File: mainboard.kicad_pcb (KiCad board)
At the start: 2 copper layers, 81.3 x 72.5 mm, 56 parts, among them J1 Screw_Terminal_1x02, Q1 SQ2309ES, U1 AT90CAN128-16MU, U2 MCP2551-I/SN, Y1 Crystal

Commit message: Did some power things
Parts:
- moved Q1 10.3 mm to (130.2, 99.7), turned to 180 degrees
- moved C9 8.55 mm to (122.2, 101.3)
- moved C3 8.52 mm to (122.2, 102.7)
- moved R8 6.86 mm to (115.2, 100.5)
- moved D2 6.85 mm to (115.2, 105.3)
- moved J1 1.79 mm to (131.8, 104.9)
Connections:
- R8 pad 1: (no net) -> +5V
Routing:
- net +5V: track 265.4 -> 224.8 mm, vias 13 -> 11
- net GND: track 106.5 -> 72.7 mm
- net Net-(J1-Pad2): track 7.44 -> 0.00 mm
- net Net-(D2-Pad2): track 1.85 -> 0.00 mm
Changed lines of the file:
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@@
 (kicad_pcb (version 4) (host pcbnew 4.0.6-e0-6349~53~ubuntu16.04.1)
   (general
-    (links 196)
-    (no_connects 5)
+    (links 197)
+    (no_connects 60)
     (area 62.027999 36.881999 143.458001 109.549001)
     (thickness 1.6)
     (drawings 182)
-    (tracks 629)
+    (tracks 601)
     (zones 0)
     (modules 56)
@@
   )
   (module Connectors_Terminal_Blocks:TerminalBlock_Pheonix_MPT-2.54mm_2pol (layer F.Cu)
-    (at 130.18 105.712 180)
+    (at 131.78 104.912 180)
     (descr "2-way 2.54mm pitch terminal block, Phoenix MPT series")
     (fp_text reference J1 (at 1.27 -4.50088 180) (layer F.SilkS) hide
@@
   )
   (module LEDs:LED_1206 (layer F.Cu)
-    (at 108.331 105.029 90)
+    (at 115.18 105.312 90)
     (descr "LED 1206 smd package")
     (tags "LED led 1206 SMD smd SMT smt smdled SMDLED smtled SMTLED")
@@
   )
   (module Resistors_SMD:R_1206 (layer F.Cu)
-    (at 108.331 100.076 270)
+    (at 115.18 100.512 270)
     (descr "Resistor SMD 1206, reflow soldering, Vishay (see dcrcw.pdf)")
     (tags "resistor 1206")
@@
     (fp_line (start 2.15 1.1) (end 2.15 -1.11) (layer F.CrtYd) (width 0.05))
     (fp_line (start 2.15 1.1) (end -2.15 1.1) (layer F.CrtYd) (width 0.05))
-    (pad 1 smd rect (at -1.45 0 270) (size 0.9 1.7) (layers F.Cu F.Paste F.Mask))
+    (pad 1 smd rect (at -1.45 0 270) (size 0.9 1.7) (layers F.Cu F.Paste F.Mask)
+      (net 4 +5V))
     (pad 2 smd rect (at 1.45 0 270) (size 0.9 1.7) (layers F.Cu F.Paste F.Mask)
       (net 63 "Net-(D2-Pad2)"))
@@
   )
   (module Capacitors_SMD:CP_Elec_6.3x4.5 (layer F.Cu)
-    (at 113.665 102.997 270)
+    (at 122.18 102.712 270)
     (descr "SMT capacitor, aluminium electrolytic, 6.3x4.5")
     (attr smd)
@@
   )
   (module Capacitors_THT:CP_Radial_D7.5mm_P2.50mm (layer F.Cu)
-    (at 113.665 102.108 270)
+    (at 122.18 101.312 270)
     (descr "CP, Radial series, Radial, pin pitch=2.50mm, , diameter=7.5mm, Electrolytic Capacitor")
     (tags "CP Radial series Radial pin pitch 2.50mm  diameter 7.5mm Electrolytic Capacitor")
@@
   )
   (module TO_SOT_Packages_SMD:SOT-23 (layer F.Cu)
-    (at 120.65 103.632 270)
+    (at 130.18 99.712 180)
     (descr "SOT-23, Standard")
     (tags SOT-23)
     (attr smd)
-    (fp_text reference Q1 (at -2.52 -0.13 360) (layer F.SilkS)
+    (fp_text reference Q1 (at -2.52 -0.13 270) (layer F.SilkS)
       (effects (font (size 1 1) (thickness 0.15)))
     )
-    (fp_text value SQ2309ES (at 0 2.5 270) (layer F.Fab) hide
+    (fp_text value SQ2309ES (at 0 2.5 180) (layer F.Fab) hide
       (effects (font (size 1 1) (thickness 0.15)))
     )
-    (fp_text user %R (at 0 0 360) (layer F.Fab)
+    (fp_text user %R (at 0 0 270) (layer F.Fab)
       (effects (font (size 0.5 0.5) (thickness 0.075)))
     )
@@
     (fp_line (start 0.76 -1.58) (end -1.4 -1.58) (layer F.SilkS) (width 0.12))
     (fp_line (start 0.76 1.58) (end -0.7 1.58) (layer F.SilkS) (width 0.12))
-    (pad 1 smd rect (at -1 -0.95 270) (size 0.9 0.8) (layers F.Cu F.Paste F.Mask)
+    (pad 1 smd rect (at -1 -0.95 180) (size 0.9 0.8) (layers F.Cu F.Paste F.Mask)
       (net 2 GND))
-    (pad 2 smd rect (at -1 0.95 270) (size 0.9 0.8) (layers F.Cu F.Paste F.Mask)
+    (pad 2 smd rect (at -1 0.95 180) (size 0.9 0.8) (layers F.Cu F.Paste F.Mask)
       (net 4 +5V))
-    (pad 3 smd rect (at 1 0 270) (size 0.9 0.8) (layers F.Cu F.Paste F.Mask)
+    (pad 3 smd rect (at 1 0 180) (size 0.9 0.8) (layers F.Cu F.Paste F.Mask)
       (net 64 "Net-(J1-Pad2)"))
     (model ${KISYS3DMOD}/TO_SOT_Packages_SMD.3dshapes/SOT-23.wrl
@@
   (gr_line (start 62.23 36.957) (end 143.383 36.957) (angle 90) (layer Edge.Cuts) (width 0.15))
   (gr_line (start 62.103 109.474) (end 62.103 37.084) (angle 90) (layer Edge.Cuts) (width 0.15))
-  (gr_text 5V (at 125.38 105.912 90) (layer F.SilkS)
+  (gr_text 5V (at 126.98 105.712 90) (layer F.SilkS)
     (effects (font (size 1 1) (thickness 0.1)))
   )
@@
     (effects (font (size 0.8 0.7) (thickness 0.125)))
   )
-  (gr_text GND (at 132.38 106.112 270) (layer F.SilkS)
+  (gr_text GND (at 133.98 105.512 270) (layer F.SilkS)
     (effects (font (size 1 1) (thickness 0.1)))
   )
@@
   (segment (start 64.008 80.645) (end 66.675 83.312) (width 0.25) (layer F.Cu) (net 2))
   (segment (start 64.008 64.9732) (end 63.9826 64.9478) (width 0.5) (layer F.Cu) (net 2))
-  (segment (start 121.6 102.632) (end 130.1 102.632) (width 0.5) (layer F.Cu) (net 2))
-  (segment (start 130.18 102.712) (end 130.18 105.712) (width 0.5) (layer F.Cu) (net 2))
-  (segment (start 130.1 102.632) (end 130.18 102.712) (width 0.5) (layer F.Cu) (net 2))
-  (segment (start 130.18 105.712) (end 132.78 105.712) (width 0.5) (layer F.Cu) (net 2))
-  (segment (start 141.605 102.487) (end 141.605 100.203) (width 0.5) (layer F.Cu) (net 2))
-  (segment (start 141.58 102.512) (end 141.605 102.487) (width 0.5) (layer F.Cu) (net 2))
-  (segment (start 135.98 102.512) (end 141.58 102.512) (width 0.5) (layer F.Cu) (net 2))
-  (segment (start 132.78 105.712) (end 135.98 102.512) (width 0.5) (layer F.Cu) (net 2))
   (segment (start 94.1366 99.8625) (end 99.1589 99.8625) (width 0.5) (layer F.Cu) (net 2))
   (segment (start 99.1589 99.8625) (end 99.5553 100.2589) (width 0.5) (layer F.Cu) (net 2))
-  (segment (start 108.331 106.679) (end 112.683 106.679) (width 0.5) (layer F.Cu) (net 2))
-  (segment (start 112.683 106.679) (end 113.665 105.697) (width 0.5) (layer F.Cu) (net 2))
   (segment (start 105.664 38.989) (end 109.7778 38.989) (width 0.5) (layer F.Cu) (net 2))
   (segment (start 109.7778 38.989) (end 109.855 39.0662) (width 0.5) (layer F.Cu) (net 2))
@@
   (segment (start 91.9226 99.1235) (end 93.3976 99.1235) (width 0.25) (layer F.Cu) (net 2))
   (segment (start 93.3976 99.1235) (end 94.1366 99.8625) (width 0.25) (layer F.Cu) (net 2))
-  (segment (start 112.683 106.679) (end 113.665 105.697) (width 0.25) (layer F.Cu) (net 2))
   (segment (start 100.362 78.82) (end 100.362 80.042) (width 0.25) (layer F.Cu) (net 2))
   (via (at 100.4316 80.1116) (size 0.6) (drill 0.4) (layers F.Cu B.Cu) (net 2))
@@
   (segment (start 101.981 80.556) (end 101.981 81.079) (width 0.25) (layer F.Cu) (net 3))
   (segment (start 101.962 80.537) (end 101.981 80.556) (width 0.25) (layer F.Cu) (net 3))
-  (segment (start 113.665 102.108) (end 119.176 102.108) (width 0.5) (layer F.Cu) (net 4))
-  (segment (start 119.176 102.108) (end 119.7 102.632) (width 0.5) (layer F.Cu) (net 4))
-  (segment (start 108.331 98.626) (end 111.994 98.626) (width 0.5) (layer F.Cu) (net 4))
-  (segment (start 111.994 98.626) (end 113.665 100.297) (width 0.5) (layer F.Cu) (net 4))
   (segment (start 121.666 42.164) (end 121.666 44.831) (width 0.5) (layer F.Cu) (net 4))
   (segment (start 121.666 39.497) (end 121.666 42.164) (width 0.5) (layer F.Cu) (net 4))
-  (segment (start 87.1601 101.6486) (end 87.1601 99.1235) (width 0.25) (layer F.Cu) (net 4))
-  (segment (start 108.331 97.4598) (end 108.331 98.626) (width 0.25) (layer F.Cu) (net 4))
-  (segment (start 107.8992 97.028) (end 108.331 97.4598) (width 0.25) (layer F.Cu) (net 4))
-  (via (at 107.8992 97.028) (size 0.6) (drill 0.4) (layers F.Cu B.Cu) (net 4))
-  (segment (start 89.2556 97.028) (end 107.8992 97.028) (width 0.25) (layer B.Cu) (net 4))
-  (segment (start 88.9 97.3836) (end 89.2556 97.028) (width 0.25) (layer B.Cu) (net 4))
-  (via (at 88.9 97.3836) (size 0.6) (drill 0.4) (layers F.Cu B.Cu) (net 4))
-  (segment (start 87.1601 99.1235) (end 88.9 97.3836) (width 0.25) (layer F.Cu) (net 4))
   (segment (start 97.962 63.42) (end 97.962 76.028) (width 0.25) (layer F.Cu) (net 4))
   (segment (start 99.562 80.2192) (end 99.562 78.82) (width 0.25) (layer F.Cu) (net 4))
@@
   (via (at 124.7648 52.0192) (size 0.6) (drill 0.4) (layers F.Cu B.Cu) (net 4))
   (segment (start 120.904 52.0192) (end 124.7648 52.0192) (width 0.25) (layer F.Cu) (net 4))
-  (segment (start 111.994 98.626) (end 113.665 100.297) (width 0.25) (layer F.Cu) (net 4))
   (segment (start 118.163 49.0982) (end 119.4054 49.0982) (width 0.25) (layer F.Cu) (net 4))
   (segment (start 119.8118 46.6852) (end 121.666 44.831) (width 0.25) (layer F.Cu) (net 4))
@@
   (segment (start 121.539 49.964) (end 123.358 49.964) (width 0.25) (layer F.Cu) (net 62))
   (segment (start 123.358 49.964) (end 123.444 49.878) (width 0.25) (layer F.Cu) (net 62))
-  (segment (start 108.331 101.526) (end 108.331 103.379) (width 0.5) (layer F.Cu) (net 63))
-  (segment (start 120.65 104.632) (end 120.7 104.632) (width 0.5) (layer F.Cu) (net 64))
-  (segment (start 120.7 104.632) (end 121.78 105.712) (width 0.5) (layer F.Cu) (net 64))
-  (segment (start 121.78 105.712) (end 127.64 105.712) (width 0.5) (layer F.Cu) (net 64))
   (zone (net 2) (net_name GND) (layer B.Cu) (hatch edge 0.508)
     (connect_pads (clearance 0.508))
     (min_thickness 0.254)
-    (fill yes (mode segment) (arc_segments 16) (thermal_gap 0.508) (thermal_bridge_width 0.508))
+    (fill (mode segment) (arc_segments 16) (thermal_gap 0.508) (thermal_bridge_width 0.508))
     (polygon
       (pts

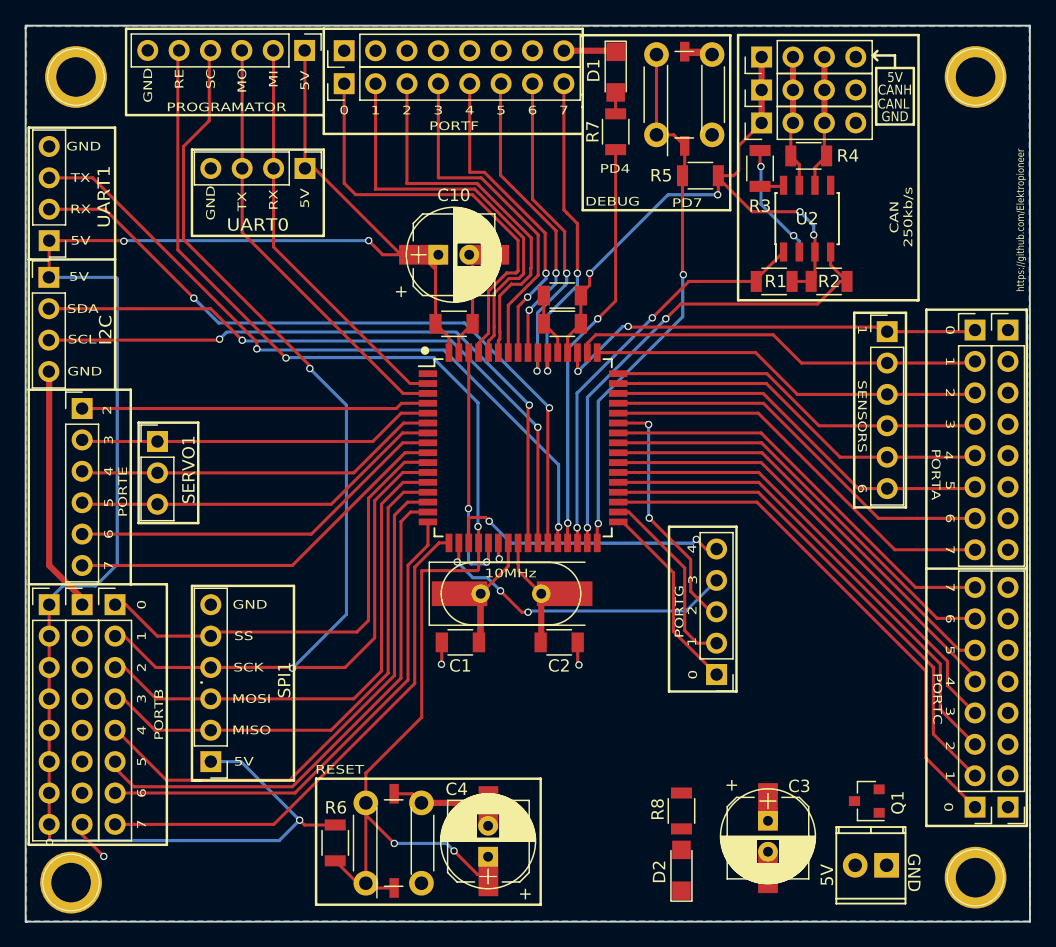
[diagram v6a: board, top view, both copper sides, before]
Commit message: Added the zone
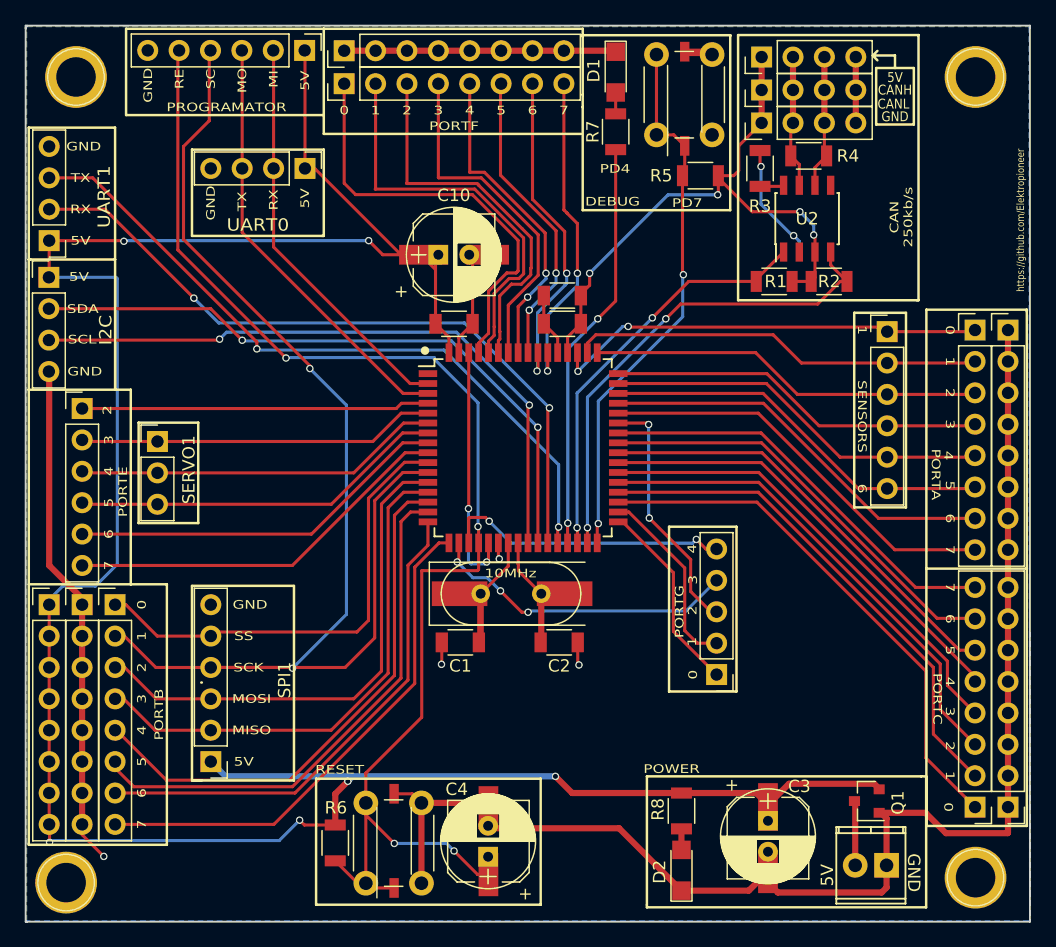
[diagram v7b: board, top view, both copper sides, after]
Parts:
- moved REF** 0.40 mm to (65.4, 106.3)
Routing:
- net GND: track 72.7 -> 214.7 mm, vias 7 -> 8
- net +5V: track 224.8 -> 276.7 mm, vias 11 -> 14
- net Net-(J1-Pad2): track 0.00 -> 5.22 mm
- net Net-(D2-Pad2): track 0.00 -> 1.70 mm
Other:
- board text added: "POWER"

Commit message: New idea around servo power and new mosfet version for protection
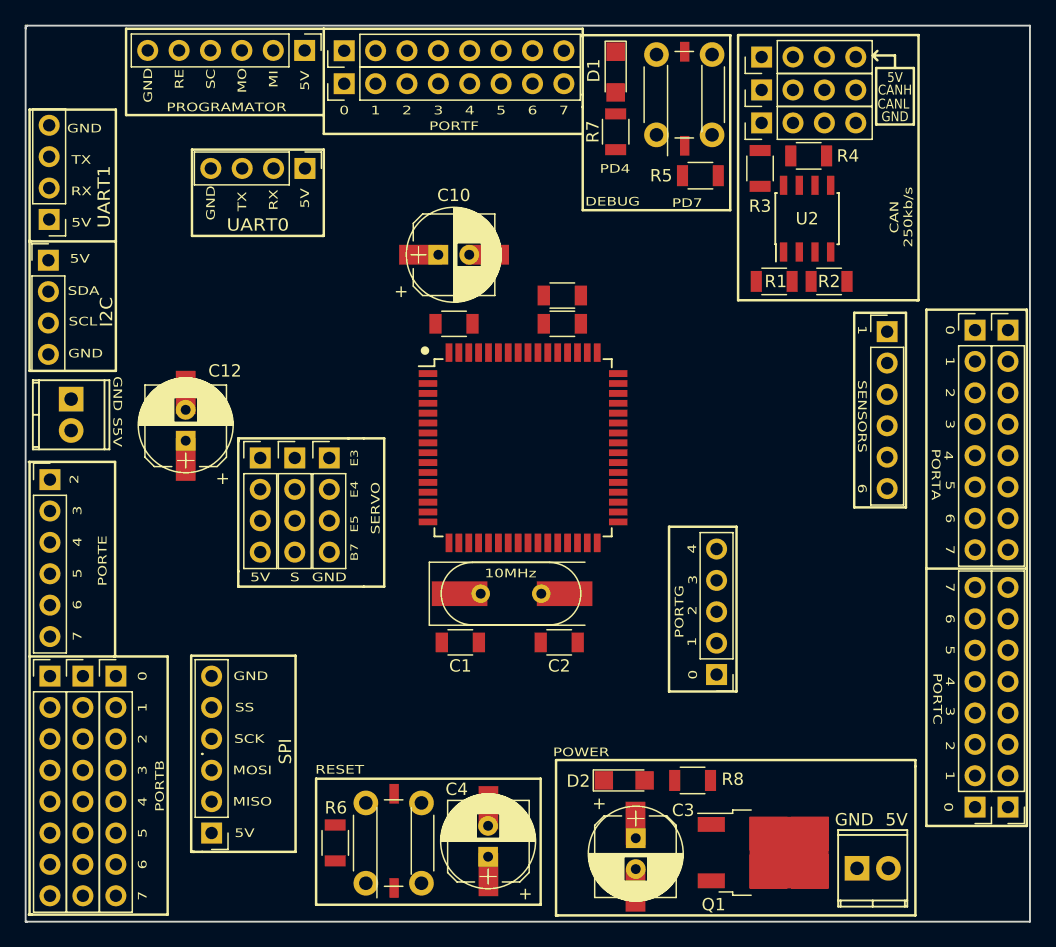
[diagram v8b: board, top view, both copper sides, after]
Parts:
- removed REF** (x4): 1pin, Connectors:1pin
- added C12: 100u, Capacitors_THT:CP_Radial_D7.5mm_P2.50mm, F.Cu at (75.1, 70.5)
- added C13: 100u, Capacitors_SMD:CP_Elec_6.3x4.5, F.Cu at (75.1, 69.3)
- added J2: SERVO 5V, Connectors_Terminal_Blocks:TerminalBlock_Pheonix_MPT-2.54mm_2pol, F.Cu at (65.8, 67.2)
- added SERO_5V1: CONN_01X04, Pin_Headers:Pin_Header_Straight_1x04_Pitch2.54mm, F.Cu at (81.1, 71.9)
- added SERVO_GND1: CONN_01X04, Pin_Headers:Pin_Header_Straight_1x04_Pitch2.54mm, F.Cu at (86.7, 71.9)
- Q1: value SQ2309ES -> IRLR024NPBF; footprint TO_SOT_Packages_SMD:SOT-23 -> TO_SOT_Packages_SMD:TO-252-2
- SERVO1: value CONN_01X03 -> CONN_01X04; footprint Pin_Headers:Pin_Header_Straight_1x03_Pitch2.54mm -> Pin_Headers:Pin_Header_Straight_1x04_Pitch2.54mm
- moved SERVO1 11.2 mm to (83.9, 71.9)
- moved C3 10.8 mm to (111.5, 104.2)
- moved C9 10.8 mm to (111.5, 102.7)
- moved Q1 9.37 mm to (121.8, 103.9), turned to 0 degrees
- moved D2 8.62 mm to (110.5, 98.0), turned to 0 degrees
- moved PE1 6.31 mm to (64.1, 73.7)
- moved PB1 5.78 mm to (69.4, 89.6)
- moved PB_GND1 5.78 mm to (66.7, 89.6)
- moved PB_VCC1 5.78 mm to (64.1, 89.6)
- moved SPI 5.78 mm to (77.2, 102.3)
- moved R8 2.63 mm to (116.1, 98.0), turned to 180 degrees
- moved J1 2.40 mm to (129.4, 105.2), turned to 0 degrees
- moved UART1 1.71 mm to (64.0, 52.6)
- moved I2C1 1.38 mm to (63.9, 55.9)
- renumbered SPI1 to SPI
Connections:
- J1 pad 1: GND -> Net-(J1-Pad1)
- J1 pad 2: Net-(J1-Pad2) -> +5V
- Q1 pad 1: GND -> +5V
- Q1 pad 2: +5V -> Net-(J1-Pad1)
- Q1 pad 3: Net-(J1-Pad2) -> GND
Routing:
- net +5V: track 276.7 -> 0.00 mm, vias 14 -> 0
- net GND: track 214.7 -> 0.00 mm, vias 8 -> 0
- net RESET: track 109.8 -> 0.00 mm, vias 4 -> 0
- net PB1: track 104.4 -> 0.00 mm, vias 2 -> 0
- net RXD1: track 58.1 -> 0.00 mm, vias 2 -> 0
- net TXD1: track 57.5 -> 0.00 mm, vias 2 -> 0
- net SDA: track 52.9 -> 0.00 mm, vias 2 -> 0
- net SCL: track 52.8 -> 0.00 mm, vias 2 -> 0
- net PD7: track 44.3 -> 0.00 mm, vias 2 -> 0
- net PB4: track 43.9 -> 0.00 mm
- net PC0: track 43.2 -> 0.00 mm
- net PB5: track 43.1 -> 0.00 mm
- net PB3: track 42.2 -> 0.00 mm
- net PB7: track 42.0 -> 0.00 mm
- net PB2: track 41.5 -> 0.00 mm
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- removed copper zone on B.Cu, net GND
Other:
- board text added: "B7"
- board text added: "E3"
- board text added: "E4"
- board text added: "E5"
- board text added: "S"
- board text added: "S5V"
- board text added: "SERVO"
- board text removed: "https://github.com/Elektropioneer"
